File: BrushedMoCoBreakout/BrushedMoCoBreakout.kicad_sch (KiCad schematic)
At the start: 19 parts, among them U1 DRV8244S

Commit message: Swap to square andersons
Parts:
- Conn1, Conn2: footprint MRDT_Connectors:Anderson_2_Horizontal_Stacked_PV -> MRDT_Connectors:Square_Anderson_2_H_Stacked_PV
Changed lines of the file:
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@@
       (effects (font (size 1.524 1.524)))
     )
-    (property "Footprint" "MRDT_Connectors:Anderson_2_Horizontal_Stacked_PV" (at 19.05 40.64 0)
+    (property "Footprint" "MRDT_Connectors:Square_Anderson_2_H_Stacked_PV" (at 19.05 40.64 0)
       (effects (font (size 1.524 1.524)) hide)
     )
@@
       (effects (font (size 1.524 1.524)) (justify right))
     )
-    (property "Footprint" "MRDT_Connectors:Anderson_2_Horizontal_Stacked_PV" (at 74.93 48.26 0)
+    (property "Footprint" "MRDT_Connectors:Square_Anderson_2_H_Stacked_PV" (at 74.93 48.26 0)
       (effects (font (size 1.524 1.524)) hide)
     )
@@
       (effects (font (size 1.524 1.524)) (justify right))
     )
-    (property "Footprint" "MRDT_Connectors:Anderson_2_Horizontal_Stacked_PV" (at 74.93 38.1 0)
+    (property "Footprint" "MRDT_Connectors:Square_Anderson_2_H_Stacked_PV" (at 74.93 38.1 0)
       (effects (font (size 1.524 1.524)) hide)
     )
@@
       (effects (font (size 1.524 1.524)))
     )
-    (property "Footprint" "MRDT_Connectors:Anderson_2_Horizontal_Stacked_PV" (at 19.05 53.34 0)
-      (effects (font (size 1.524 1.524)) hide)
-    )
+    (property "Footprint" "MRDT_Connectors:Square_Anderson_2_H_Stacked_PV" (at 19.05 53.34 0)
+      (effects (font (size 1.524 1.524)) hide)
+    )

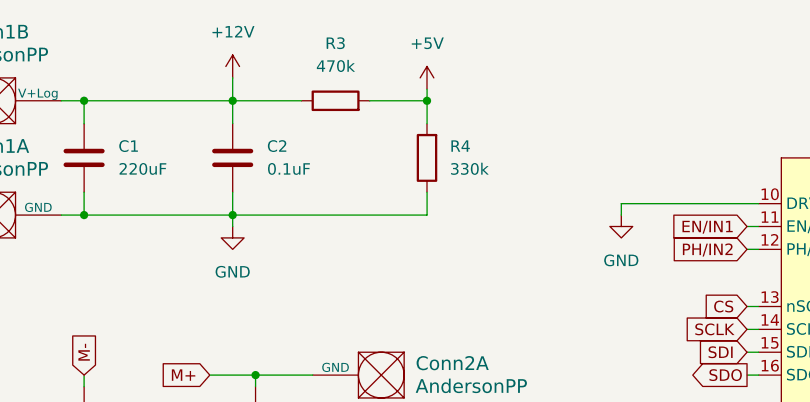
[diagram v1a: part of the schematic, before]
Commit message: Adjust resistor values
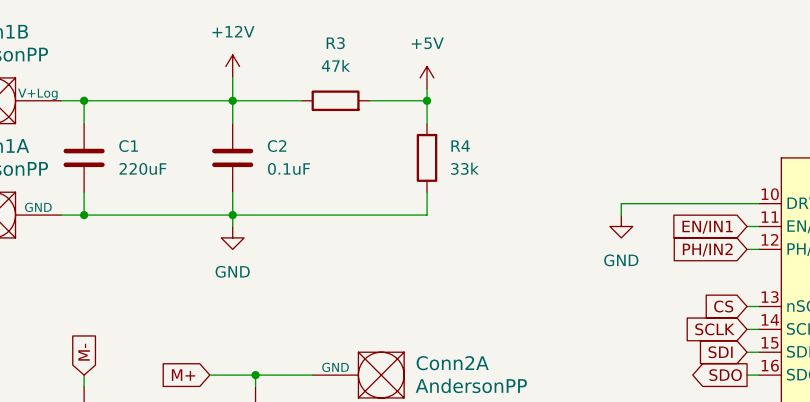
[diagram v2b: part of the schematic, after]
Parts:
- R3: value 470k -> 47k
- R4: value 330k -> 33k
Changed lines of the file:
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@@
       (effects (font (size 1.27 1.27)) (justify right))
     )
-    (property "Value" "330k" (at 76.2 31.75 0)
+    (property "Value" "33k" (at 76.2 31.75 0)
       (effects (font (size 1.27 1.27)) (justify right))
     )
@@
       (effects (font (size 1.27 1.27)))
     )
-    (property "Value" "470k" (at 63.5 20.32 90)
+    (property "Value" "47k" (at 63.5 20.32 90)
       (effects (font (size 1.27 1.27)))
     )
